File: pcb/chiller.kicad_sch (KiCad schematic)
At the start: 41 parts, among them J1 CONN_01X03, J10 CONN_01X03, J11 CONN_01X02, J12 CONN_01X02, J2 CONN_01X03, J3 CONN_01X03, J4 CONN_01X02, J5 CONN_01X02, J6 CONN_01X02, J7 CONN_01X02, J8 CONN_01X02, J9 LCD-20X4, Q1 BSS138, Q2 BSS138, Q3 ZXMN4A06G, Q4 BSS138, U1 78M05, U2 Arduino_Nano_v3.x

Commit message: Start designing new PCB.
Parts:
- removed C1: 10u, Capacitor_SMD:C_0805_2012Metric, symbol chiller-rescue:CP
- removed C2, C3, C4: 100n, Capacitor_SMD:C_0603_1608Metric, symbol chiller-rescue:C
- removed C5, C6: 10u, Capacitor_SMD:C_0805_2012Metric, symbol chiller-rescue:C
- removed D1: BAT54, Package_TO_SOT_SMD:SOT-23, symbol Diode:BAT54C
- removed D2: SS34, Diode_SMD:D_SMC, symbol tinkerforge:D
- removed J1, J10, J2, J3: CONN_01X03, Connector_JST:JST_XH_B03B-XH-A_1x03_P2.50mm_Vertical, symbol chiller-rescue:CONN_01X03
- removed J11, J12, J4, J5, J6, J7, J8: CONN_01X02, Connector_JST:JST_XH_B02B-XH-A_1x02_P2.50mm_Vertical, symbol tinkerforge:CONN_01X02
- removed J9: LCD-20X4, Connector_PinHeader_2.54mm:PinHeader_1x16_P2.54mm_Vertical, symbol tinkerforge:LCD-20X4
- removed Q1, Q2, Q4: BSS138, Package_TO_SOT_SMD:SOT-23, symbol Transistor_FET:BSS138
- removed Q3: ZXMN4A06G, Package_TO_SOT_SMD:SOT-223-3_TabPin2, symbol Transistor_FET:BSP129
- removed R1: 100, Resistor_SMD:R_0603_1608Metric, symbol chiller-rescue:R
- removed R10, R4, R6, R8: 1K, Resistor_SMD:R_0603_1608Metric, symbol chiller-rescue:R
- removed R11, R12, R13, R5, R7, R9: 10K, Resistor_SMD:R_0603_1608Metric, symbol chiller-rescue:R
- removed R2, R3: 4K7, Resistor_SMD:R_0603_1608Metric, symbol chiller-rescue:R
- removed RL1: G6B-1114C-US5DC, modules:DIL-relay, symbol omron:G6B-1114C-US5DC
- removed RV1: 10K, Potentiometer_SMD:Potentiometer_Vishay_TS53YL_Vertical, symbol chiller-rescue:POT_TRIM
- removed U1: 78M05, modules:DPAK-3, symbol chiller-rescue:7805
- removed U2: Arduino_Nano_v3.x, Module:Arduino_Nano, symbol MCU_Module:Arduino_Nano_v3.x
- added C1: 1uF, Capacitor_SMD:C_0603_1608Metric, symbol Device:C_Small
- added C2: 10uF, Capacitor_SMD:C_0603_1608Metric_Pad1.08x0.95mm_HandSolder, symbol Device:C_Small
- added D1: 1N4148, Diode_SMD:D_SOD-123, symbol Device:D_Small
- added D2: LED, LED_SMD:LED_0603_1608Metric, symbol Device:LED
- added F1: 250mA, modules:Fuseholder5x20_horiz_SemiClosed_Casing10x25mm, symbol Device:Fuse_Small
- added H1, H2, H3, H4: MountingHole, MountingHole:MountingHole_3.2mm_M3, symbol Mechanical:MountingHole
- added J1: Current Sense, Connector_JST:JST_XH_B3B-XH-A_1x03_P2.50mm_Vertical, symbol Connector_Generic:Conn_01x03
- added J2: Conn_01x14, symbol Connector_Generic:Conn_01x14
- added J3: Mains, Connector_Phoenix_MSTB:PhoenixContact_MSTBVA_2,5_2-G-5,08_1x02_P5.08mm_Vertical, symbol Connector_Generic:Conn_01x02
- added J4: Debug, Connector_PinHeader_2.54mm:PinHeader_1x06_P2.54mm_Vertical, symbol Connector_Generic:Conn_01x06
- added J5, J8: Conn_01x03, symbol Connector_Generic:Conn_01x03
- added J6: Relay, Connector_Phoenix_MSTB:PhoenixContact_MSTBVA_2,5_3-G-5,08_1x03_P5.08mm_Vertical, symbol Connector_Generic:Conn_01x03
- added J7: Ext, Connector_PinHeader_2.54mm:PinHeader_1x05_P2.54mm_Vertical, symbol Connector_Generic:Conn_01x05
- added K1: G5LE-1, Relay_THT:Relay_SPDT_Omron-G5LE-1, symbol Relay:G5LE-1
- added PS1: HLK-PM01, Converter_ACDC:Converter_ACDC_HiLink_HLK-PMxx, symbol Converter_ACDC:HLK-PM01
- added Q1, Q2: MMBT3904, Package_TO_SOT_SMD:SOT-23, symbol Transistor_BJT:MMBT3904
- added Q3: BSS138, Package_TO_SOT_SMD:SOT-323_SC-70, symbol Device:Q_NMOS_GSD
- added Q4: MMBT3906, Package_TO_SOT_SMD:SOT-23, symbol Transistor_BJT:MMBT3906
- added R1, R7: 1k, Resistor_SMD:R_0603_1608Metric, symbol Device:R_Small
- added R2, R8: 10k, Resistor_SMD:R_0603_1608Metric, symbol Device:R_Small
- added R3: 1k2, Resistor_SMD:R_0603_1608Metric, symbol Device:R_Small
- added R4: 2k2, Resistor_SMD:R_0603_1608Metric, symbol Device:R_Small
- added R6: 1K5, Resistor_SMD:R_0603_1608Metric, symbol Device:R
- added SW1: Card switch, Connector_JST:JST_XH_B2B-XH-A_1x02_P2.50mm_Vertical, symbol Switch:SW_SPST
- added TP11: TestPoint, TestPoint:TestPoint_Keystone_5000-5004_Miniature, symbol Connector:TestPoint
- added U1: ESP32-WROOM-32, RF_Module:ESP32-WROOM-32, symbol RF_Module:ESP32-WROOM-32
- added U2: AP1117-33, Package_TO_SOT_SMD:SOT-223-3_TabPin2, symbol Regulator_Linear:AP1117-33
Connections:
- net +5V: now also C1.1, D1.1 (K), D2.2 (A), J1.1 (Pin_1), J4.3 (Pin_3), K1.5, PS1.4 (+Vout), Q4.2 (E), R2.1, U2.3 (VI)
- net GND: now also C1.2, C2.2, J1.3 (Pin_3), J2.2 (Pin_2), J4.1 (Pin_1), J7.5 (Pin_5), PS1.3 (-Vout), Q3.2 (S), R4.2, R8.2, TP11.1, U1.1 (GND), U1.15 (GND), U1.38 (GND), U1.39 (GND), U2.1 (GND)
- new net: F1.2, PS1.1 (AC/L)
- new net: J3.1 (Pin_1), PS1.2 (AC/N)
- new net: F1.1, J3.2 (Pin_2)
- new net: Q3.1 (G), R7.2
- new net: D1.2 (A), K1.2, Q3.3 (D), R6.2
- new net: Q4.1 (B), R1.1, R2.2
- new net: J4.4 (Pin_4), R3.1
- new net: D2.1 (K), R6.1
- new net +3V3: C2.1, J2.1 (Pin_1), J7.1 (Pin_1), SW1.2 (B), U1.2 (VDD), U2.2 (VO)
- new net COM: J6.2 (Pin_2), K1.1
- new net CurrentSense: J1.2 (Pin_2), U1.5 (SENSOR_VN)
- new net Display_A0: U1.24 (IO2)
- new net Display_CS: J2.3 (Pin_3), U1.23 (IO15)
- new net Display_DC: J2.5 (Pin_5)
- new net Display_Led: J2.8 (Pin_8), Q4.3 (C)
- new net Display_Reset: J2.4 (Pin_4), U1.26 (IO4)
- new net Display_SCk: J2.7 (Pin_7), U1.30 (IO18)
- new net Display_SDA: U1.37 (IO23)
- new net Display_SDI: J2.6 (Pin_6)
- new net Display_SDO: J2.9 (Pin_9)
- new net Display_backlight: R1.2, U1.13 (IO14)
- new net Ext1: J7.4 (Pin_4), U1.16 (IO13)
- new net Ext2: J7.3 (Pin_3), U1.11 (IO26)
- new net Ext3: J7.2 (Pin_2), U1.12 (IO27)
- new net MCU_RX0: R3.2, R4.1, U1.34 (RXD0/IO3)
- new net MCU_TX0: J4.5 (Pin_5), U1.35 (TXD0/IO1)
- new net NC: J6.1 (Pin_1), K1.4
- new net NO: J6.3 (Pin_3), K1.3
- new net card_switch: SW1.1 (A), U1.10 (IO25)
- new net relay: R7.1, R8.1
- new net relay_gpio: U1.27 (IO16)
- new net ~{BOOT}: Q1.3 (C), U1.25 (IO0)
- new net ~{DTR}: J4.6 (Pin_6), Q1.2 (E), Q2.1 (B)
- new net ~{RESET}: Q2.3 (C), U1.3 (EN)
- new net ~{RTS}: J4.2 (Pin_2), Q1.1 (B), Q2.2 (E)
- no-connect marks 15 -> 21
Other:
- note added: "Connectors"
- note added: "HV"
- note added: "LV"
- note added: "MCU"
- note added: "MSP4020"
- note added: "PSU"
- note added: "Power switching"
- note added: "Reset logic"
- note added: "Temp sensor 1"
- note added: "Temp sensor 2"
- note added: "debug"
- note removed: "BUZZER"
- note removed: "CURRENT SENSE"
- note removed: "FAN"
- note removed: "FLOW"
- note removed: "POWER"
- note removed: "PUMP"
- note removed: "Ready"
- note removed: "SERIAL"
- note removed: "SSR"
- note removed: "TEMP1"
- note removed: "TEMP2"

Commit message: Add components.
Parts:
- removed D1: 1N4148, Diode_SMD:D_SOD-123, symbol Device:D_Small
- removed D2: LED, LED_SMD:LED_0603_1608Metric, symbol Device:LED
- removed F1: 250mA, modules:Fuseholder5x20_horiz_SemiClosed_Casing10x25mm, symbol Device:Fuse_Small
- removed J3: Mains, Connector_Phoenix_MSTB:PhoenixContact_MSTBVA_2,5_2-G-5,08_1x02_P5.08mm_Vertical, symbol Connector_Generic:Conn_01x02
- removed J6: Relay, Connector_Phoenix_MSTB:PhoenixContact_MSTBVA_2,5_3-G-5,08_1x03_P5.08mm_Vertical, symbol Connector_Generic:Conn_01x03
- removed K1: G5LE-1, Relay_THT:Relay_SPDT_Omron-G5LE-1, symbol Relay:G5LE-1
- removed PS1: HLK-PM01, Converter_ACDC:Converter_ACDC_HiLink_HLK-PMxx, symbol Converter_ACDC:HLK-PM01
- removed Q3: BSS138, Package_TO_SOT_SMD:SOT-323_SC-70, symbol Device:Q_NMOS_GSD
- removed R7: 1k, Resistor_SMD:R_0603_1608Metric, symbol Device:R_Small
- removed R8: 10k, Resistor_SMD:R_0603_1608Metric, symbol Device:R_Small
- removed SW1: Card switch, Connector_JST:JST_XH_B2B-XH-A_1x02_P2.50mm_Vertical, symbol Switch:SW_SPST
- added C3: 1u, Capacitor_SMD:C_0603_1608Metric, symbol Device:C
- added C4: 10u, Capacitor_SMD:C_0603_1608Metric, symbol Device:C
- added D3, D4: 1N4148, Diode_SMD:D_SOD-123, symbol Device:D
- added J10, J11, J9: Conn_01x02, Connector_Phoenix_MSTB:PhoenixContact_MSTBA_2,5_2-G-5,08_1x02_P5.08mm_Horizontal, symbol Connector_Generic:Conn_01x02
- added J12, J13: Conn_01x02, Connector_JST:JST_XH_B2B-XH-A_1x02_P2.50mm_Vertical, symbol Connector_Generic:Conn_01x02
- added J14: CONN_01X02, Connector_JST:JST_XH_B2B-XH-A_1x02_P2.50mm_Vertical, symbol Connector_Generic:Conn_01x02
- added K2: G5LE-1, Relay_THT:Relay_SPDT_Omron-G5LE-1, symbol Relay:G5LE-1
- added Q5, Q6: BSS138, Package_TO_SOT_SMD:SOT-23, symbol Device:Q_NMOS_GSD
- added R5: 10k, Resistor_SMD:R_0603_1608Metric, symbol Device:R
- added R7: 10K, Resistor_SMD:R_0603_1608Metric, symbol Device:R
- added R8: 1K, Resistor_SMD:R_0603_1608Metric, symbol Device:R
- added RL1: G6B-1114C-US5DC, modules:DIL-relay, symbol g6b-1114c-us-dc5:G6B-1114C-US-DC5
- added U3: DSN-MINI-360, modules:DSN-MINI-360, symbol dsnmini360:DSN-MINI-360
- J2: footprint (none) -> Connector_PinSocket_2.54mm:PinSocket_1x14_P2.54mm_Vertical
- J5, J8: footprint (none) -> Connector_JST:JST_XH_B3B-XH-A_1x03_P2.50mm_Vertical
- R6: value 1K5 -> 1k
- renumbered TP11 to TP1
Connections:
- net relay_gpio is gone; now on net Relay_comp: U1.27 (IO16)
- net +5V: now also C3.1, C4.1, D3.1 (K), D4.1 (K), K2.5, RL1.2, U3.OUT+
- net GND: now also C3.2, C4.2, Q6.2 (S), R7.2
- net Relay_comp: now reaches R6.2
- net at R6.1: now also Q5.1 (G), R5.1
- new net: Q6.1 (G), R7.1, R8.1
- new net: D4.2 (A), Q6.3 (D), RL1.1
- new net: J11.1 (Pin_1), K2.1
- new net: D3.2 (A), K2.2, Q5.3 (D)
- new net: J10.1 (Pin_1), J9.1 (Pin_1), K2.3
- new net: J12.1 (Pin_1), J13.1 (Pin_1), U3.IN+
- new net: J14.1 (Pin_1), RL1.4
- new net: J14.2 (Pin_2), RL1.3
- new net: J10.2 (Pin_2), J11.2 (Pin_2), J9.2 (Pin_2)
- new net GNDS: J12.2 (Pin_2), J13.2 (Pin_2), Q5.2 (S), R5.2, U3.IN-, U3.OUT-
- new net Relay_ready: R8.2
- no-connect marks 21 -> 22
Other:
- note added: "12V in"
- note added: "Compressor"
- note added: "Mains in"
- note added: "Mains out"
- note added: "Pump"
- note added: "Ready"
- note removed: "HV"
- note removed: "LV"
- note removed: "MCU"
- note removed: "PSU"
- note removed: "Power switching"
- moved on the sheet: C1, C2, U2

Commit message: Move display connections, etc.
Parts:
- removed Q4: MMBT3906, Package_TO_SOT_SMD:SOT-23, symbol Transistor_BJT:MMBT3906
- removed R1: 1k, Resistor_SMD:R_0603_1608Metric, symbol Device:R_Small
- removed R2: 10k, Resistor_SMD:R_0603_1608Metric, symbol Device:R_Small
- added R1: 4k7, Resistor_SMD:R_0603_1608Metric, symbol Device:R
- renumbered C3 to C2, C4 to C3, C2 to C4, D3 to D1, D4 to D2, J5 to J1, J1 to J10, J2 to J11, J4 to J12, J8 to J2, J7 to J3, J9 to J4, J10 to J5, J11 to J6, J12 to J7, J13 to J8, J14 to J9, K2 to K1, RL1 to K2, Q6 to Q3, Q5 to Q4, R3 to R2, R4 to R3, R7 to R4, R8 to R6, R6 to R7, U3 to U2, U2 to U3
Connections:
- net Display_A0 is gone; now on net Display_DC: U1.24 (IO2)
- net Display_Led is gone; now on net +3V3: J11.8 (Pin_8)
- net Display_SDA is gone; now on net Display_SDI: U1.37 (IO23)
- net +3V3: now also J1.1 (Pin_1), J2.1 (Pin_1), R1.1
- net Display_CS: now also U1.29 (IO5); no longer U1.23 (IO15)
- net Display_SDO: now also U1.31 (IO19)
- net GND: now also J1.3 (Pin_3), J2.3 (Pin_3)
- net Relay_ready: now also U1.33 (IO21)
- net TempSensor: now reaches J2.2 (Pin_2)
- net TempSensor: now also J1.2 (Pin_2), U1.23 (IO15), R1.2
- net Display_SCk renamed Display_SCK
- net Display_backlight: no longer names the net of U1.13 (IO14)
- net card_switch: no longer names the net of U1.10 (IO25)
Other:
- note removed: "Connectors"
- note removed: "debug"

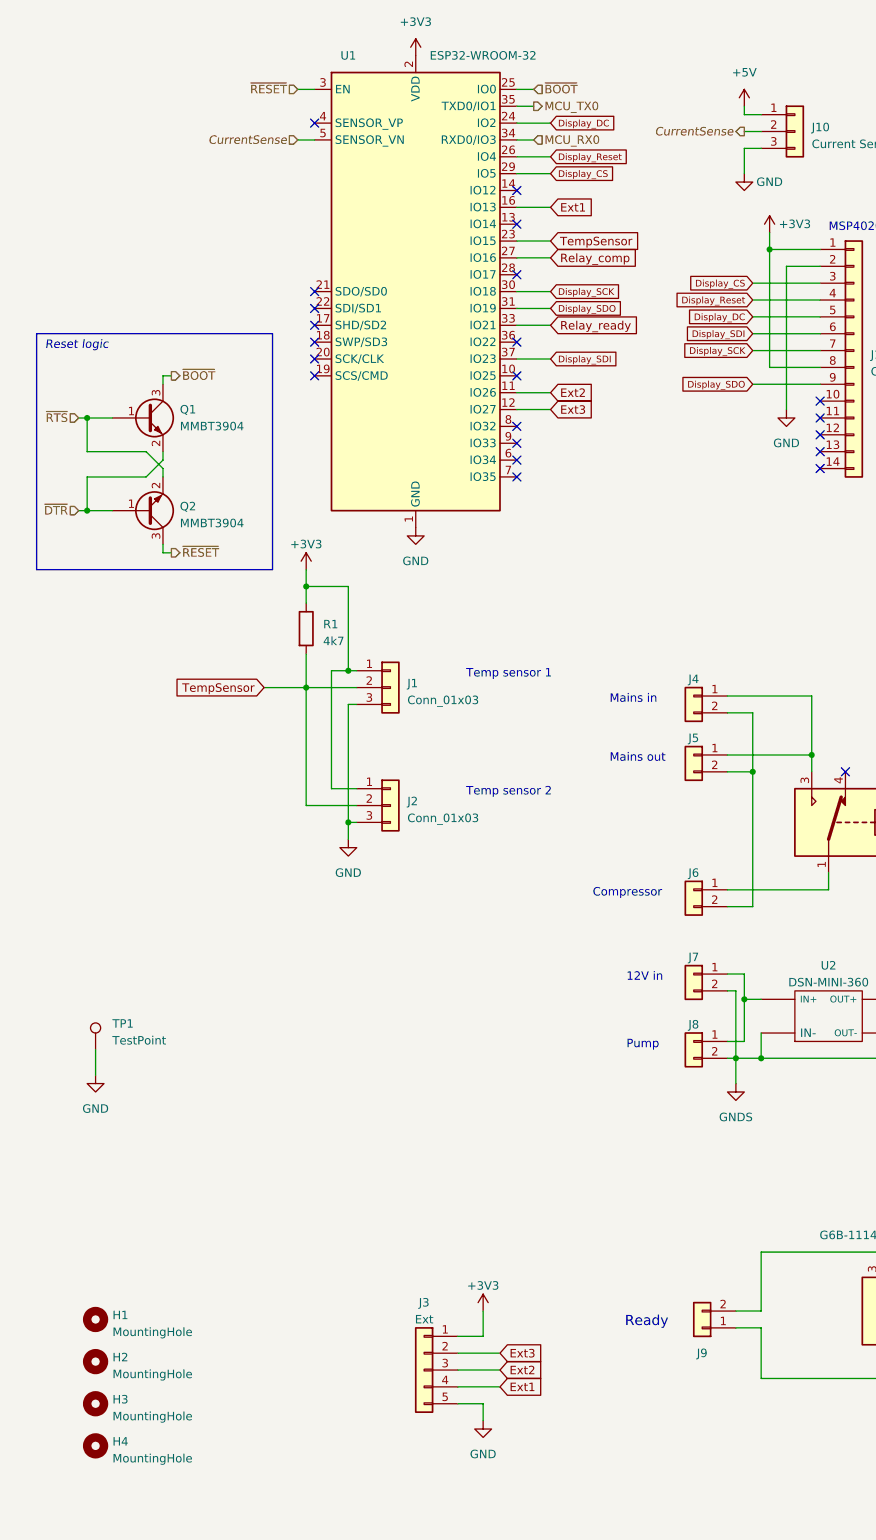
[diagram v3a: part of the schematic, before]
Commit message: Complete routing.
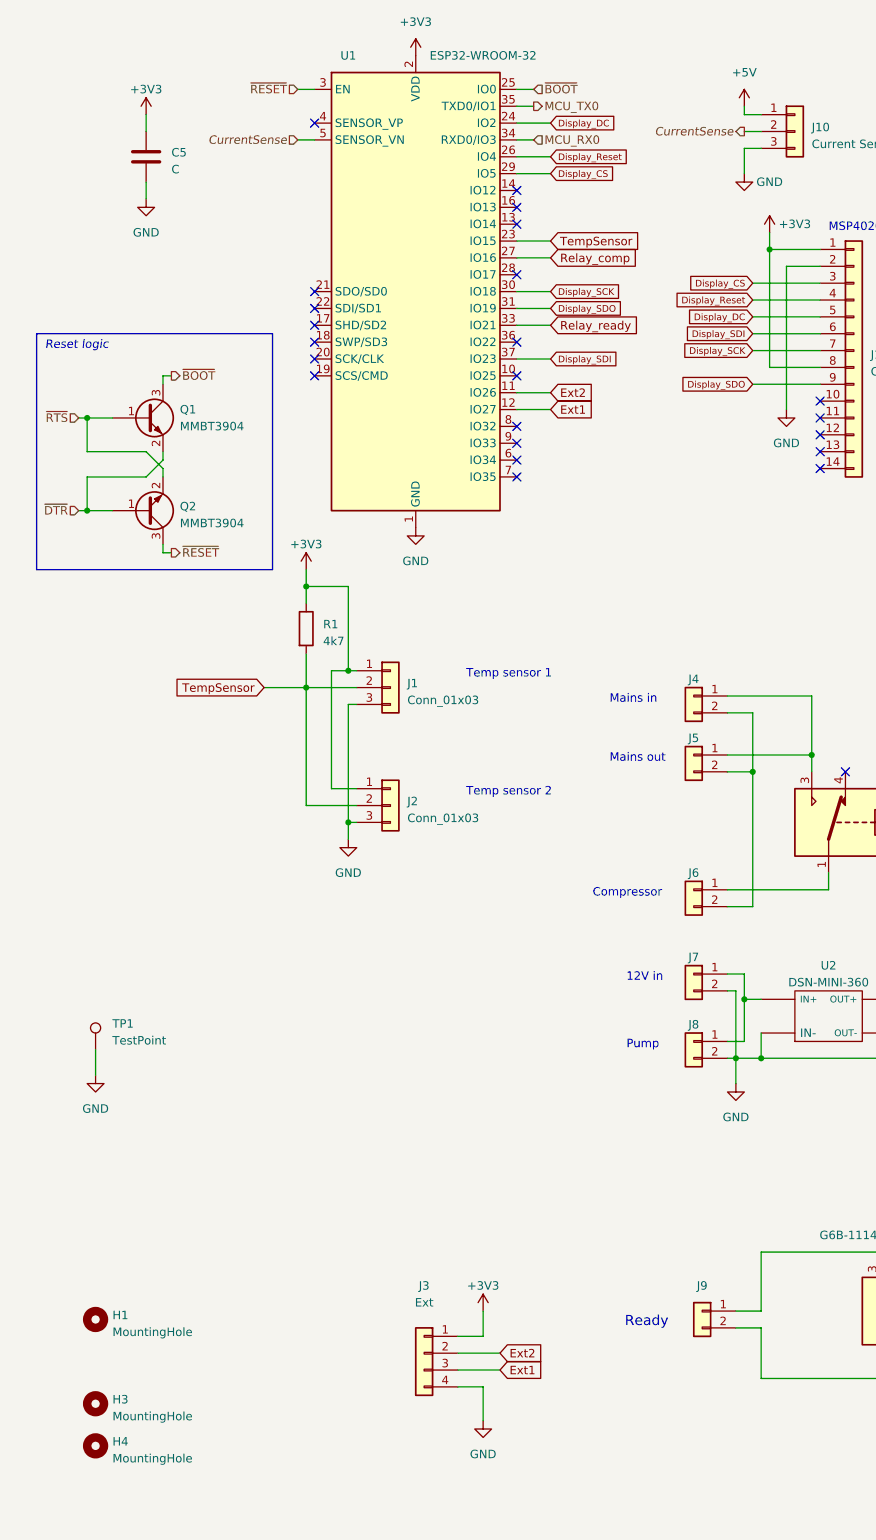
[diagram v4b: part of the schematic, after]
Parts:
- removed H2: MountingHole, MountingHole:MountingHole_3.2mm_M3, symbol Mechanical:MountingHole
- added C5: C, Capacitor_SMD:C_0603_1608Metric, symbol Device:C
- C4: footprint Capacitor_SMD:C_0603_1608Metric_Pad1.08x0.95mm_HandSolder -> Capacitor_SMD:C_0603_1608Metric
- J3: footprint Connector_PinHeader_2.54mm:PinHeader_1x05_P2.54mm_Vertical -> Connector_PinHeader_2.54mm:PinHeader_1x04_P2.54mm_Vertical; symbol Connector_Generic:Conn_01x05 -> Connector_Generic:Conn_01x04
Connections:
- net GNDS is gone; now on net GND: J7.2 (Pin_2), J8.2 (Pin_2), Q4.2 (S), R5.2, U2.IN-, U2.OUT-
- net +3V3: now also C5.1
- net Ext1: now also J3.3 (Pin_3), U1.12 (IO27); no longer J3.4 (Pin_4), U1.16 (IO13)
- net Ext2: now also J3.2 (Pin_2); no longer J3.3 (Pin_3)
- net GND: now also J3.4 (Pin_4), C5.2; no longer J3.5 (Pin_5)
- net at J9.1 (Pin_1): now also K2.3; no longer K2.4
- net at J9.2 (Pin_2): now also K2.4; no longer K2.3
- removed net Ext3: J3.2 (Pin_2), U1.12 (IO27)
- no-connect marks 22 -> 23
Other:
- moved on the sheet: J9
